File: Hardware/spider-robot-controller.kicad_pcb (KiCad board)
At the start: 2 copper layers, 26 parts, among them CON1 AVR-ISP-6, CON2 BARREL_JACK, IC1 ATMEGA328-P, P1 SERVO_HEADER, P10 SERVO_HEADER, P11 SERVO_HEADER, P12 SERVO_HEADER, P13 Bluetooth_header, P2 SERVO_HEADER, P3 SERVO_HEADER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

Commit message: working on pcb
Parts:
- added D1: LED, LEDs:LED-5MM, B.Cu at (135.9, 45.7)
- added P14: CONN_01X01, Pin_Headers:Pin_Header_Straight_1x01, B.Cu at (118.7, 52.1)
- added P15: CONN_01X01, Pin_Headers:Pin_Header_Straight_1x01, B.Cu at (127.0, 60.3)
- added P16: CONN_01X01, Pin_Headers:Pin_Header_Straight_1x01, B.Cu at (102.2, 52.1)
- added P17: CONN_01X01, Pin_Headers:Pin_Header_Straight_1x01, B.Cu at (127.0, 65.4)
- added P18: CONN_01X01, Pin_Headers:Pin_Header_Straight_1x01, B.Cu at (140.3, 79.4)
- added P19: CONN_01X01, Pin_Headers:Pin_Header_Straight_1x01, B.Cu at (139.7, 74.3)
- added P20: CONN_01X01, Pin_Headers:Pin_Header_Straight_1x01, B.Cu at (139.7, 62.9)
- added P21: CONN_01X01, Pin_Headers:Pin_Header_Straight_1x01, B.Cu at (139.7, 66.7)
- added R4: 330, Resistors_ThroughHole:Resistor_Horizontal_RM10mm, B.Cu at (141.6, 50.8)
- added SW2: SWITCH_INV, library:SWITCH_INVERTER, B.Cu at (92.7, 83.2)
- moved P6 101.8 mm to (110.7, 45.7)
- moved R3 101.1 mm to (83.8, 45.1), turned to 180 degrees
- moved P13 89.0 mm to (86.4, 40.6), turned to 270 degrees
- moved P5 89.0 mm to (104.5, 79.4), turned to 90 degrees
- moved R2 85.3 mm to (98.4, 47.0), turned to 180 degrees
- moved P2 80.0 mm to (107.2, 45.7)
- moved P7 73.0 mm to (127.0, 45.7)
- moved P1 69.7 mm to (104.5, 83.0), turned to 90 degrees
- moved P4 58.1 mm to (130.7, 77.9), turned to 270 degrees
- moved P10 53.1 mm to (114.3, 45.7)
- moved P9 49.6 mm to (104.5, 75.9), turned to 90 degrees
- moved CON1 49.3 mm to (130.8, 62.9), turned to 270 degrees
- moved R1 40.8 mm to (119.4, 91.4)
- moved P8 36.0 mm to (130.7, 81.4), turned to 270 degrees
- moved P3 32.0 mm to (123.2, 45.7)
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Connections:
- CON2 pad 1: Net-(C3-Pad2) -> Net-(CON2-Pad1)
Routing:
- net VCC: track 43.2 -> 158.9 mm
- net BTX: track 0.00 -> 115.2 mm
- net MOSI: track 0.00 -> 47.2 mm
- net RST: track 15.9 -> 56.5 mm
- net BRX: track 0.00 -> 39.7 mm
- net Net-(C3-Pad2): track 0.00 -> 34.9 mm
- net S4: track 0.00 -> 23.4 mm
- net S5: track 0.00 -> 20.8 mm
- net S7: track 0.00 -> 19.9 mm
- net S9: track 0.00 -> 18.5 mm
- net S6: track 0.00 -> 18.1 mm
- net SCK: track 0.00 -> 13.6 mm
- net S8: track 0.00 -> 12.7 mm
- net S1: track 0.00 -> 10.8 mm
- net S2: track 0.00 -> 10.4 mm
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- added copper zone on F.Cu, net GND

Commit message: improved pcb layout traces
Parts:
- added P22: CONN_01X01, Pin_Headers:Pin_Header_Straight_1x01, B.Cu at (127.0, 75.7)
- added P23: CONN_01X01, Pin_Headers:Pin_Header_Straight_1x01, B.Cu at (135.9, 72.4)
- added P24: CONN_01X01, Pin_Headers:Pin_Header_Straight_1x01, B.Cu at (98.4, 61.0)
- added P25: CONN_01X01, Pin_Headers:Pin_Header_Straight_1x01, B.Cu at (92.1, 61.0)
- added P26: CONN_01X01, Pin_Headers:Pin_Header_Straight_1x01, B.Cu at (118.9, 39.6)
- added P27: CONN_01X01, Pin_Headers:Pin_Header_Straight_1x01, B.Cu at (119.4, 49.3)
- moved C3 4.45 mm to (85.1, 69.2)
- moved P20 4.14 mm to (141.0, 66.8)
- moved P19 4.06 mm to (135.9, 75.7)
- moved P21 3.81 mm to (135.9, 66.8)
- moved P14 2.41 mm to (116.3, 52.1)
- moved C1 1.91 mm to (100.3, 69.2)
- moved C2 1.91 mm to (100.3, 64.1)
- moved CON1 1.91 mm to (130.8, 61.0)
- moved Y1 1.91 mm to (107.3, 66.7)
- moved P18 1.53 mm to (141.0, 80.8)
- moved P12 1.40 mm to (130.8, 86.4)
- moved P4 1.40 mm to (130.8, 79.2)
- moved P8 1.40 mm to (130.8, 82.8)
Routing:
- net VCC: track 158.9 -> 190.5 mm
- net RST: track 56.5 -> 64.4 mm
- net Net-(C1-Pad2): track 13.9 -> 12.0 mm
- net Net-(C2-Pad2): track 13.9 -> 12.1 mm
- net SCK: track 13.6 -> 15.1 mm
- net S7: track 19.9 -> 21.0 mm
- net S10: track 8.87 -> 9.72 mm
- net MISO: track 8.89 -> 9.68 mm
- net S12: track 9.50 -> 10.2 mm
- net S11: track 9.08 -> 9.78 mm
- net BRX: track 39.7 -> 39.1 mm
- net Net-(C3-Pad2): track 34.9 -> 34.3 mm

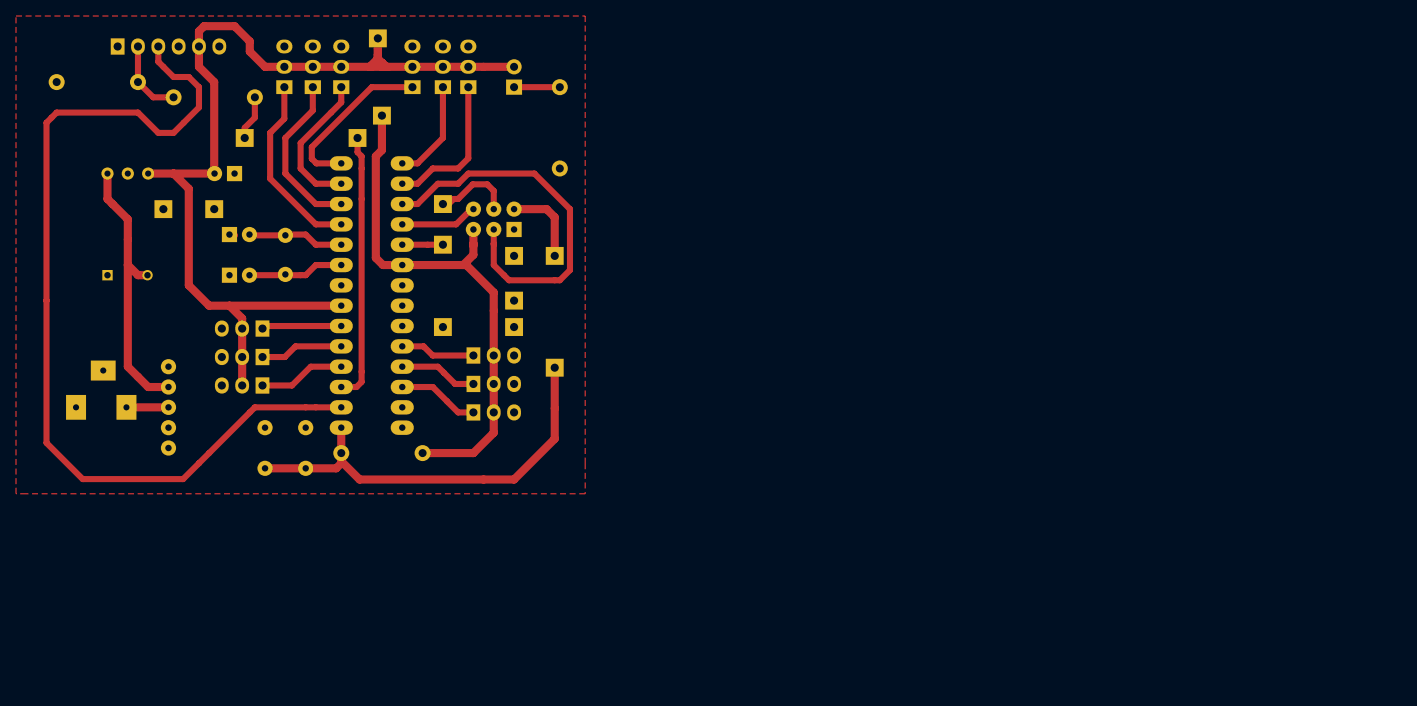
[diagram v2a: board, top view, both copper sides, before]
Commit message: Changed from single board to a shield
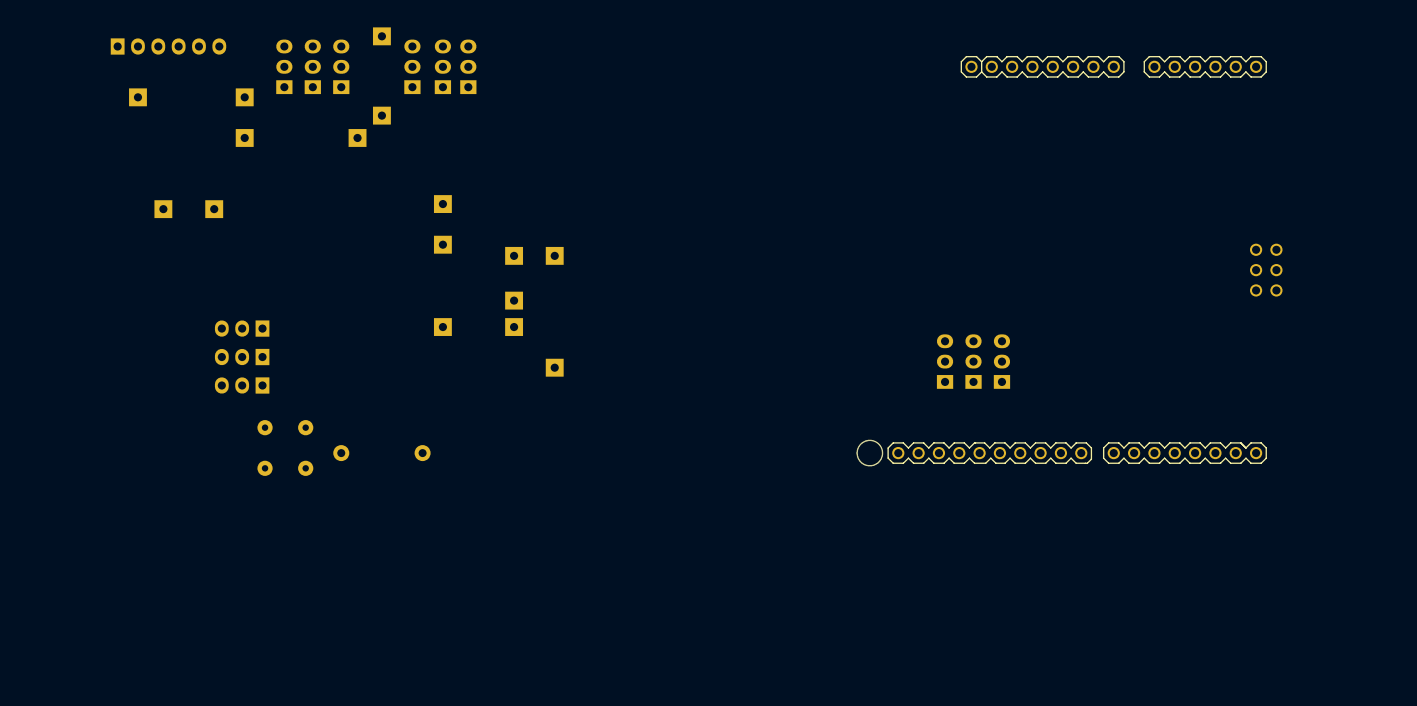
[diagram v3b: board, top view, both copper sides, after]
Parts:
- removed C1, C2: 22pF, Capacitors_ThroughHole:C_Disc_D3_P2.5
- removed C3: 100nF, Capacitors_ThroughHole:C_Radial_D10_L13_P5
- removed C4: 10nF, Capacitors_ThroughHole:C_Radial_D5_L6_P2.5
- removed CON1: AVR-ISP-6, Pin_Headers:Pin_Header_Straight_2x03
- removed CON2: BARREL_JACK, library:BARREL_JACK
- removed D1: LED, LEDs:LED-5MM
- removed IC1: ATMEGA328-P, library:ATMEGA328P-PU
- removed R2, R4: 330, Resistors_ThroughHole:Resistor_Horizontal_RM10mm
- removed R3: 660, Resistors_ThroughHole:Resistor_Horizontal_RM10mm
- removed SW2: SWITCH_INV, library:SWITCH_INVERTER
- removed U1: LM7805, library:LM7805
- removed Y1: 16MHz, Crystals:Crystal_HC49-U_Vertical
- added P28: CONN_01X01, Pin_Headers:Pin_Header_Straight_1x01, B.Cu at (102.2, 47.0)
- added P29: CONN_01X01, Pin_Headers:Pin_Header_Straight_1x01, B.Cu at (88.9, 47.0)
- added SHIELD1: ARDUINO_SHIELD, freetronics_footprints:ARDUINO_SHIELD_ROUNDPADS, B.Cu at (165.1, 40.6)
- moved P12 66.1 mm to (196.8, 82.5), turned to 0 degrees
- moved P8 62.5 mm to (193.3, 82.5), turned to 0 degrees
- moved P4 59.0 mm to (189.7, 82.5), turned to 0 degrees
- moved P26 0.57 mm to (119.4, 39.4)
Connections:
- P13 pad 2: Net-(P13-Pad2) -> BRX
- P13 pad 6: Net-(P13-Pad6) -> VCC
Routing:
- net VCC: track 190.5 -> 0.00 mm
- net BTX: track 115.2 -> 0.00 mm
- net RST: track 64.4 -> 0.00 mm
- net MOSI: track 47.4 -> 0.00 mm
- net BRX: track 39.1 -> 0.00 mm
- net Net-(C3-Pad2): track 34.3 -> 0.00 mm
- net S4: track 23.4 -> 0.00 mm
- net S7: track 21.0 -> 0.00 mm
- net S5: track 20.8 -> 0.00 mm
- net S9: track 18.5 -> 0.00 mm
- net S6: track 18.1 -> 0.00 mm
- net SCK: track 15.1 -> 0.00 mm
- net S8: track 12.7 -> 0.00 mm
- net Net-(C2-Pad2): track 12.1 -> 0.00 mm
- net Net-(C1-Pad2): track 12.0 -> 0.00 mm
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- removed copper zone on F.Cu, net GND

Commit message: Improvements on the shield
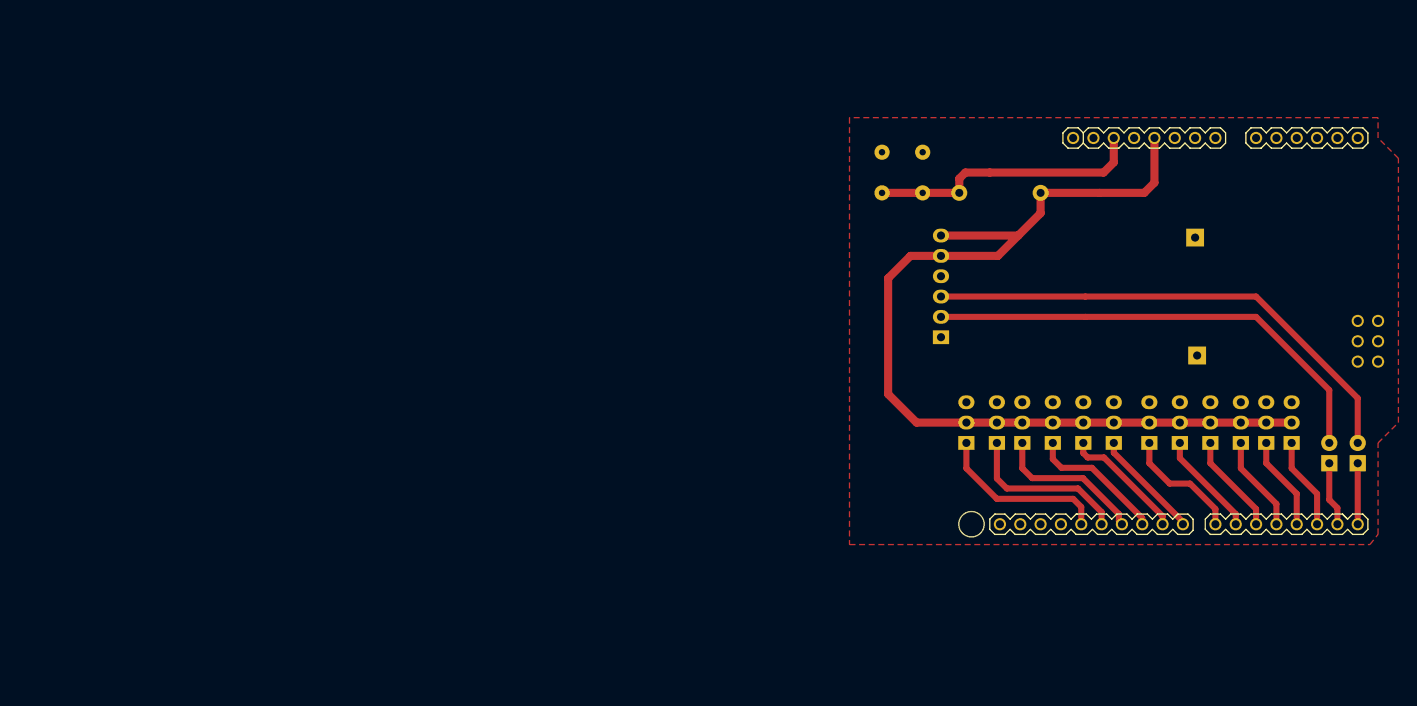
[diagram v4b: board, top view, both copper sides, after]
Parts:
- removed P14, P15, P16, P17, P18, P19, P20, P21, P22, P23, P26, P27, P28, P29: CONN_01X01, Pin_Headers:Pin_Header_Straight_1x01
- added JP1: JUMPER, Pin_Headers:Pin_Header_Straight_1x02, B.Cu at (237.7, 92.7)
- added JP2: JUMPER, Pin_Headers:Pin_Header_Straight_1x02, B.Cu at (241.3, 92.7)
- P13: footprint Pin_Headers:Pin_Header_Straight_1x06 -> Pin_Headers:Pin_Header_Angled_1x06
- moved P25 129.0 mm to (221.0, 64.5)
- moved P1 128.8 mm to (233.0, 90.2), turned to 0 degrees
- moved P5 125.9 mm to (229.9, 90.2), turned to 0 degrees
- moved P24 124.2 mm to (221.2, 79.2)
- moved P2 123.9 mm to (222.9, 90.2)
- moved P9 123.1 mm to (226.7, 90.2), turned to 0 degrees
- moved P6 117.1 mm to (219.1, 90.2)
- moved P10 110.3 mm to (215.3, 90.2)
- moved P13 109.1 mm to (189.2, 77.0), turned to 0 degrees
- moved P3 98.3 mm to (210.8, 90.2)
- moved P7 91.5 mm to (207.0, 90.2)
- moved P11 85.5 mm to (203.2, 90.2)
- moved SW1 84.4 mm to (186.9, 58.9)
- moved R1 83.8 mm to (196.6, 58.9)
- moved SHIELD1 15.5 mm to (177.8, 49.5)
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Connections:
- P13 pad 2: BRX -> Net-(P13-Pad2)
- P13 pad 3: BTX -> Net-(P13-Pad3)
- SHIELD1 pad 0: BTX -> Net-(JP2-Pad1)
- SHIELD1 pad 1: BRX -> Net-(JP1-Pad1)
- SHIELD1 pad 5V: Net-(SHIELD1-Pad5V) -> VCC
- SHIELD1 pad RST: Net-(SHIELD1-PadRST) -> RST
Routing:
- net VCC: track 0.00 -> 121.3 mm
- net Net-(P13-Pad3): track 0.00 -> 57.3 mm
- net Net-(P13-Pad2): track 0.00 -> 52.3 mm
- net RST: track 0.00 -> 34.6 mm
- net S12: track 0.00 -> 21.7 mm
- net S11: track 0.00 -> 20.8 mm
- net S10: track 0.00 -> 19.0 mm
- net S9: track 0.00 -> 17.0 mm
- net S8: track 0.00 -> 15.5 mm
- net S6: track 0.00 -> 15.1 mm
- net S7: track 0.00 -> 13.7 mm
- net S5: track 0.00 -> 13.1 mm
- net S4: track 0.00 -> 12.5 mm
- net S3: track 0.00 -> 12.0 mm
- net S2: track 0.00 -> 11.7 mm
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- added copper zone on F.Cu, net GND
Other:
- net class Default: clearance 0.5842 -> 0.53
- net class POWER: clearance 0.5842 -> 0.53
- rule trace_clearance: 0.5842 -> 0.53

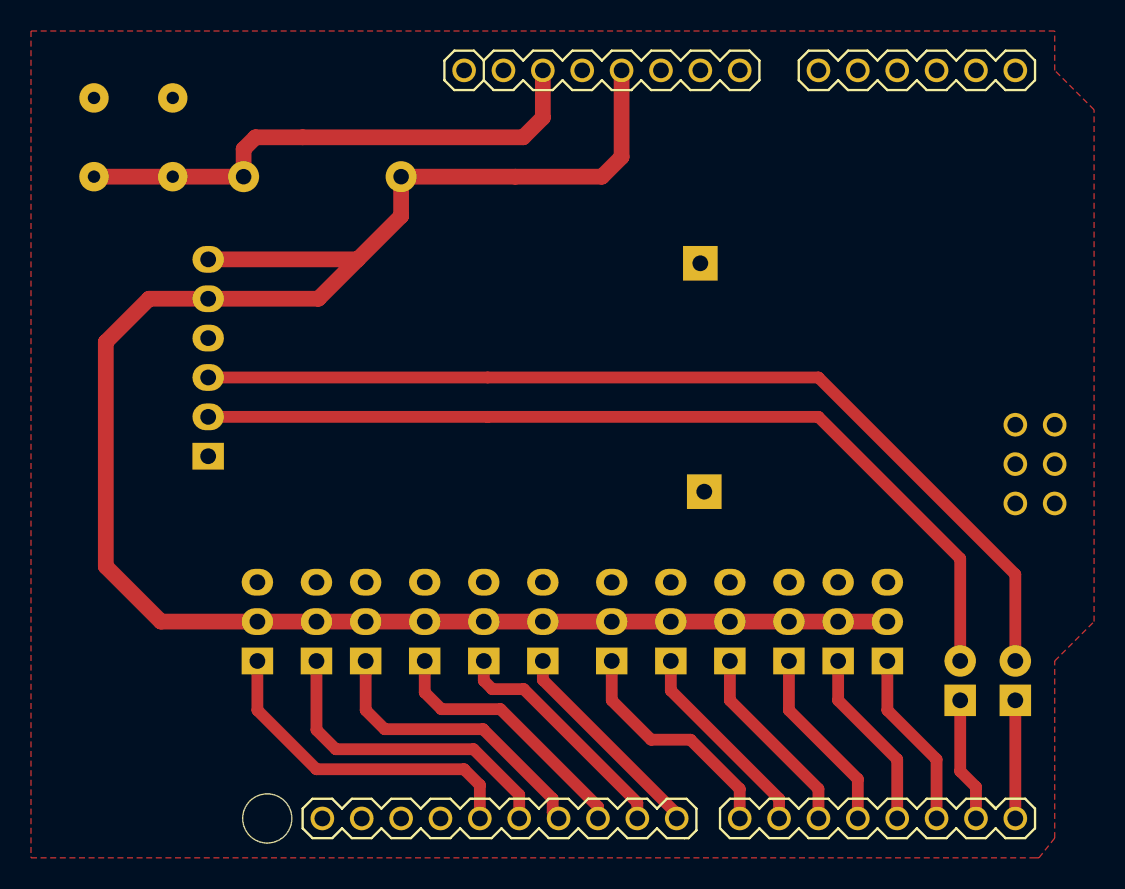
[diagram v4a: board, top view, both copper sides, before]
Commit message: Added leds at bluetooth serial traces
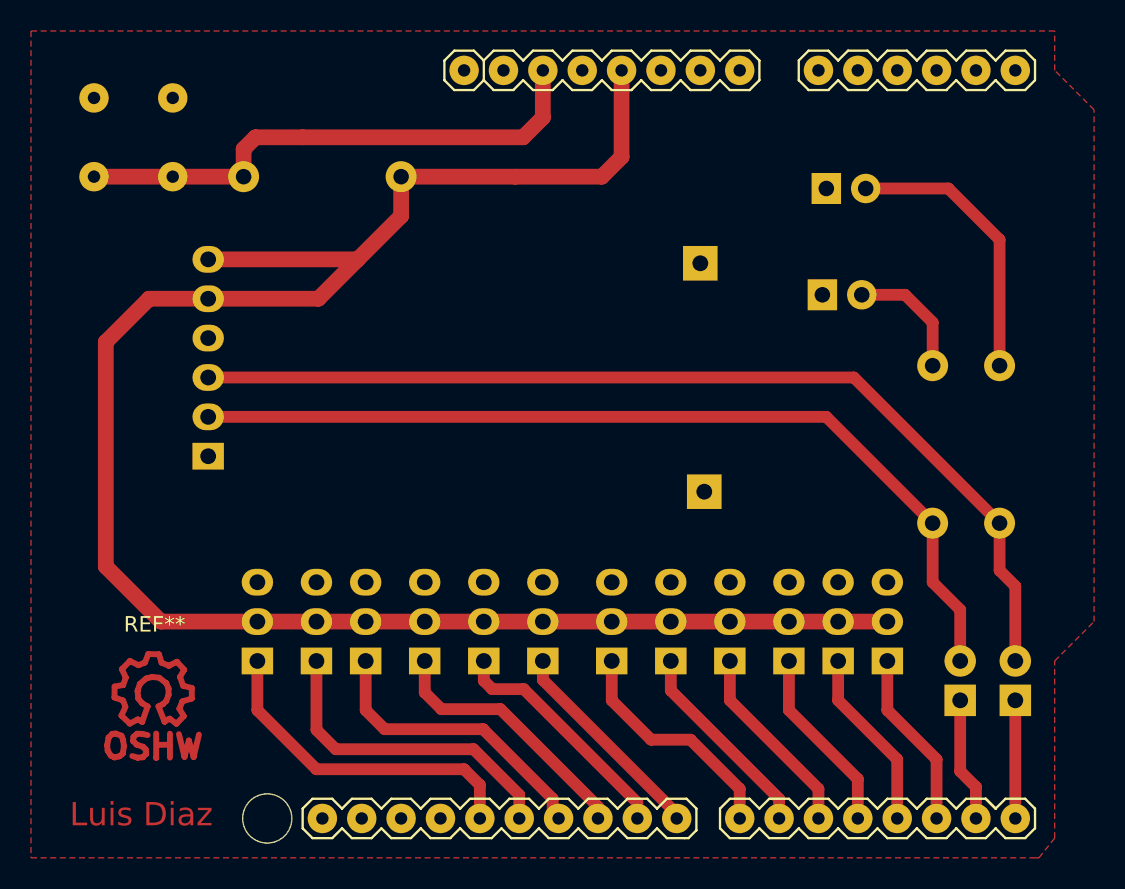
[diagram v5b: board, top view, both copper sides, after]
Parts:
- added D1: LED-TX, LEDs:LED-5MM, B.Cu at (229.1, 59.7)
- added D2: LED-RX, LEDs:LED-5MM, B.Cu at (228.9, 66.5)
- added R2: 330, Resistors_ThroughHole:Resistor_Horizontal_RM10mm, B.Cu at (240.3, 76.2)
- added R3: 330, Resistors_ThroughHole:Resistor_Horizontal_RM10mm, B.Cu at (236.0, 76.2)
- added REF**: Symbol_OSHW-Logo_CopperTop, Symbols:Symbol_OSHW-Logo_CopperTop, F.Cu at (185.7, 92.2)
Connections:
- P13 pad 2: Net-(P13-Pad2) -> BRX
- P13 pad 3: Net-(P13-Pad3) -> BTX
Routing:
- net BTX: track 5.59 -> 64.3 mm
- net Net-(P13-Pad3): track 57.3 -> 0.00 mm
- net BRX: track 6.60 -> 59.2 mm
- net Net-(P13-Pad2): track 52.3 -> 0.00 mm
- net Net-(D1-Pad2): track 0.00 -> 18.1 mm
- net Net-(D2-Pad2): track 0.00 -> 8.10 mm
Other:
- board text added: "Luis Diaz"
